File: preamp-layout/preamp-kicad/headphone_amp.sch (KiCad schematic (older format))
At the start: 23 parts, among them J72 Conn_01x04_Male, J73 Conn_01x03_Male, J74 Conn_01x03_Male, J75 Conn_01x03_Male, J76 Conn_01x03_Female, J77 Conn_01x04_Female, U20 TPA6120

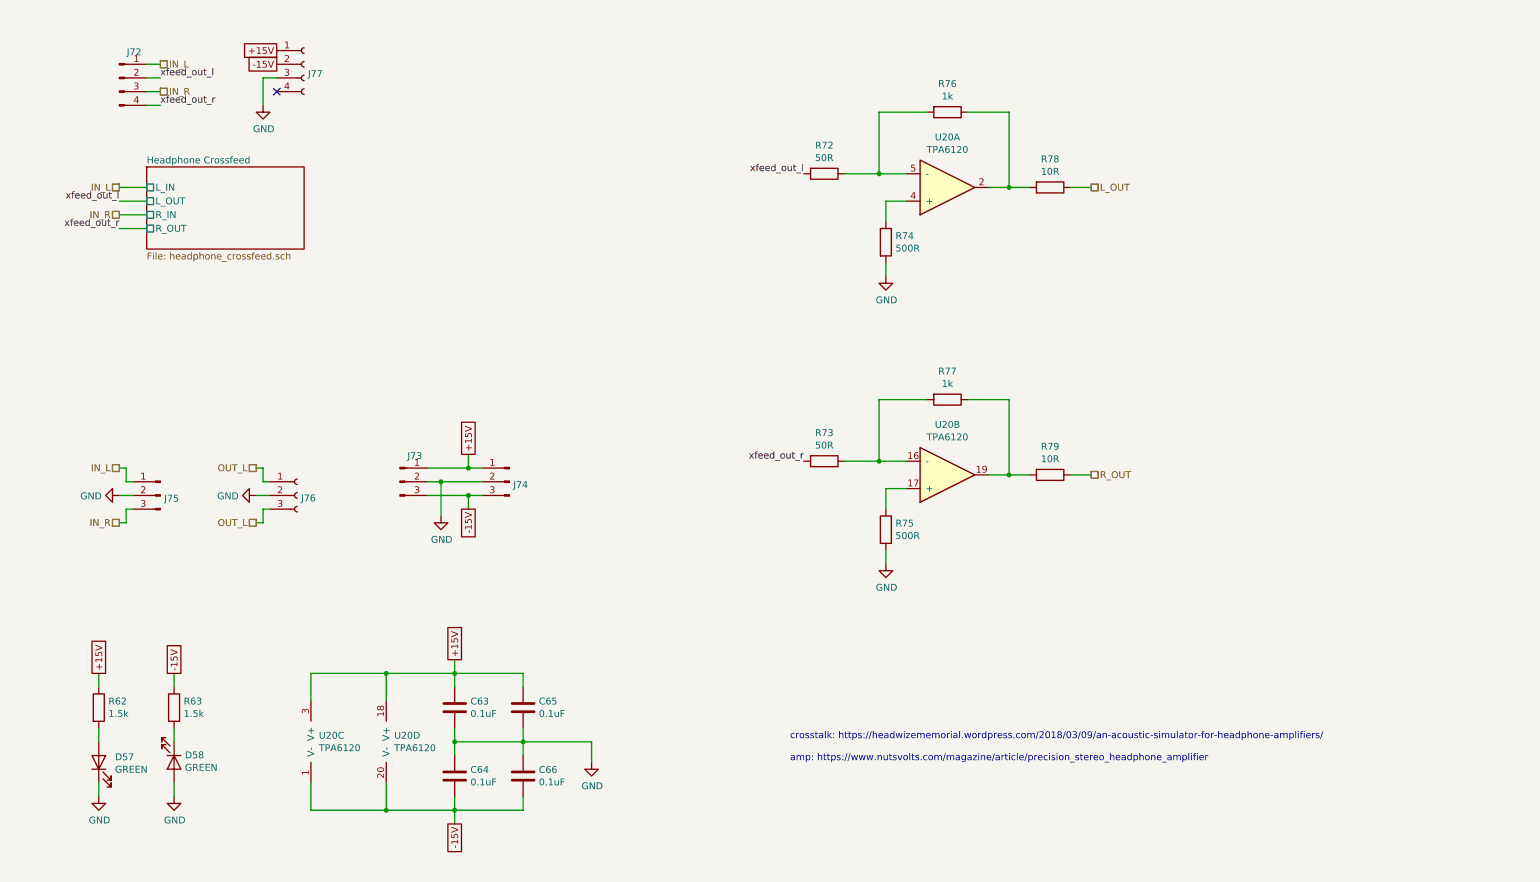
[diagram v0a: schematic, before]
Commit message: Schematic layout updates
schematic optimization. Also implemented encoders with surrounding circuitry (self-contained on encoder board)
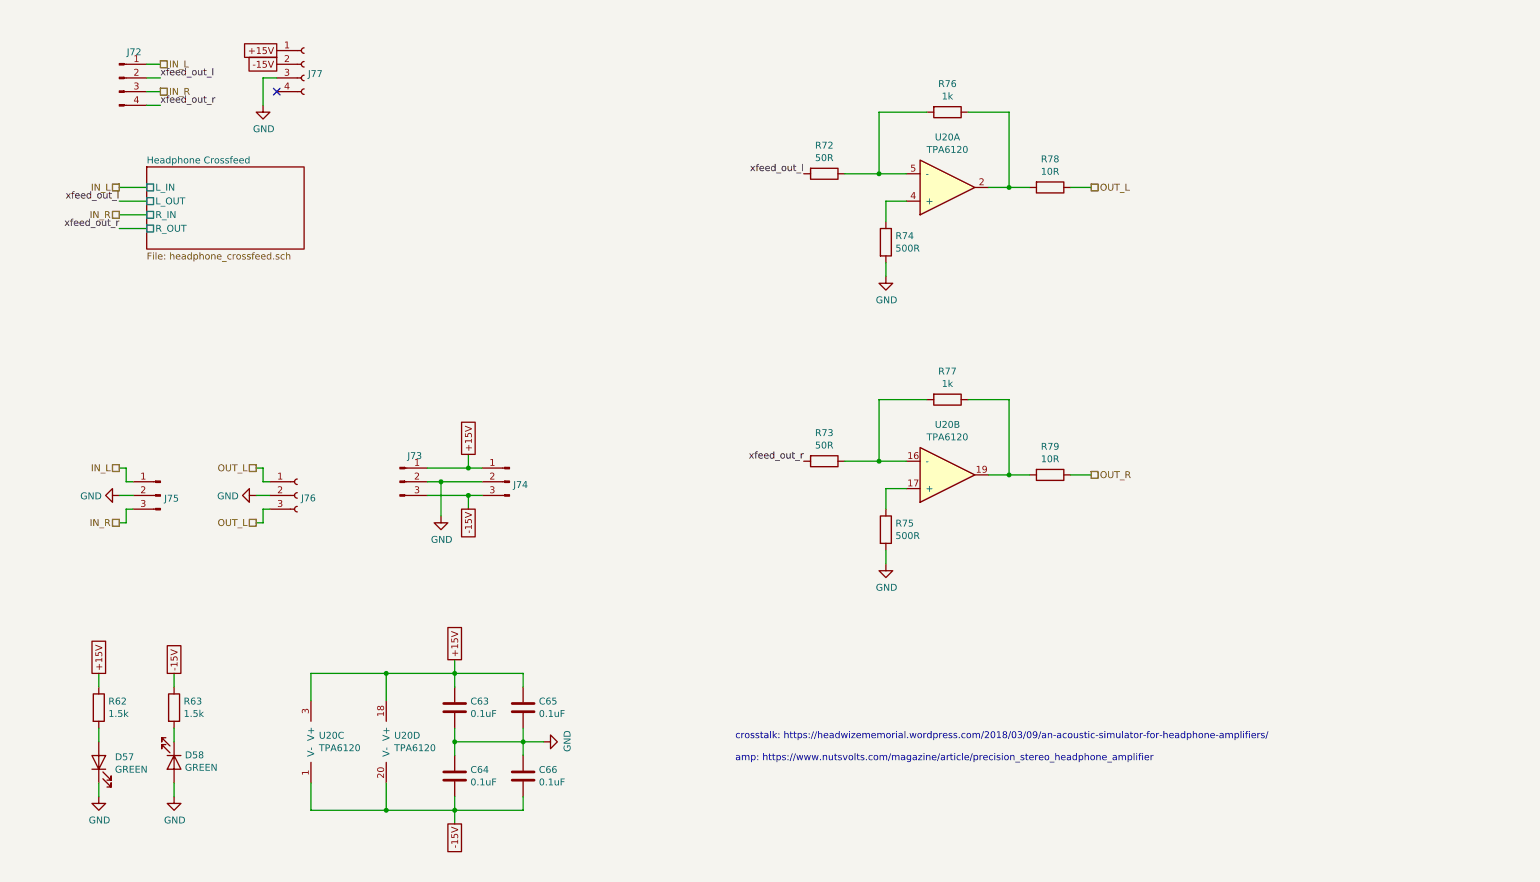
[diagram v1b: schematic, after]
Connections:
- net L_OUT is gone; now on net OUT_L: R78.1
- net R_OUT renamed OUT_R
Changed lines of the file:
@@
 Wire Wire Line
 	8550 4350 8700 4350
-Text Notes 6950 6450 0    50   ~ 0
+Text Notes 6550 6450 0    50   ~ 0
 crosstalk: https://headwizememorial.wordpress.com/2018/03/09/an-acoustic-simulator-for-headphone-amplifiers/\n\namp: https://www.nutsvolts.com/magazine/article/precision_stereo_headphone_amplifier
 Wire Wire Line
@@
 	9000 4350 9150 4350
 Text HLabel 9150 2250 2    50   UnSpc ~ 0
-L_OUT
+OUT_L
 Text HLabel 9150 4350 2    50   UnSpc ~ 0
-R_OUT
+OUT_R
 $Comp
 L preamp:TPA6120 U20
@@
 L power:GND #PWR?
 U 1 1 5F00DE46
-P 5500 6450
+P 5150 6300
 AR Path="/6009D432/5F00DE46" Ref="#PWR?"  Part="1"
 AR Path="/5E4A803E/5F00DE46" Ref="#PWR0142"  Part="1"
-F 0 "#PWR0142" H 5500 6200 50  0001 C CNN
-F 1 "GND" H 5505 6277 50  0000 C CNN
-F 2 "" H 5500 6450 50  0001 C CNN
-F 3 "" H 5500 6450 50  0001 C CNN
-	1    5500 6450
-	1    0    0    -1
+F 0 "#PWR0142" H 5150 6050 50  0001 C CNN
+F 1 "GND" H 5155 6127 50  0000 C CNN
+F 2 "" H 5150 6300 50  0001 C CNN
+F 3 "" H 5150 6300 50  0001 C CNN
+	1    5150 6300
+	0    -1   -1   0
 $EndComp
 Text HLabel 3050 4700 0    50   UnSpc ~ 0
@@
 Wire Wire Line
 	4000 5800 3450 5800
-Wire Wire Line
-	5000 6300 5500 6300
-Wire Wire Line
-	5500 6300 5500 6450
 Text HLabel 2350 1350 2    50   UnSpc ~ 0
 IN_L
@@
 Wire Wire Line
 	4600 4300 4700 4300
+Wire Wire Line
+	5000 6300 5150 6300
 $EndSCHEMATC

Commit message: Sheet cleanup
pin names reassigned, standardized. Organized sheets to reduce clutter, increase readability.
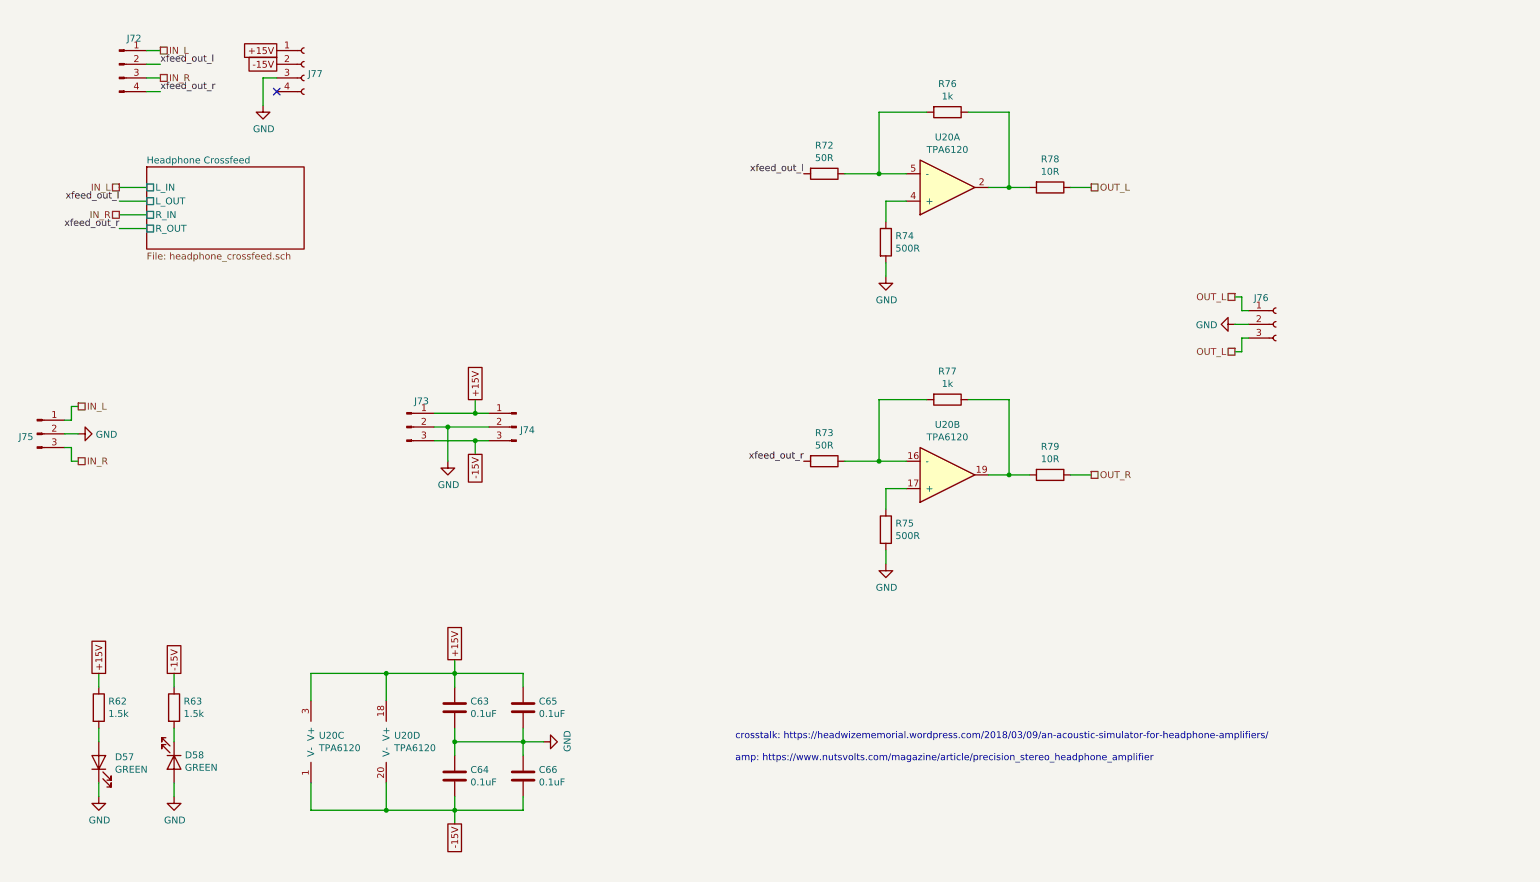
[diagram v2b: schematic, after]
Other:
- moved on the sheet: J72, J73, J74, J75, J76
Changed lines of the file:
@@
 L Connector:Conn_01x03_Male J?
 U 1 1 647A3EBE
-P 4100 4400
+P 4150 4000
 AR Path="/5E27B612/647A3EBE" Ref="J?"  Part="1"
 AR Path="/6009D432/647A3EBE" Ref="J?"  Part="1"
 AR Path="/5E4A803E/647A3EBE" Ref="J73"  Part="1"
-F 0 "J73" H 4208 4589 50  0000 C CNN
-F 1 "Conn_01x03_Male" H 4072 4333 50  0001 R CNN
-F 2 "Connector_JST:JST_EH_B3B-EH-A_1x03_P2.50mm_Vertical" H 4100 4400 50  0001 C CNN
-F 3 "~" H 4100 4400 50  0001 C CNN
-	1    4100 4400
+F 0 "J73" H 4258 4189 50  0000 C CNN
+F 1 "Conn_01x03_Male" H 4122 3933 50  0001 R CNN
+F 2 "Connector_JST:JST_EH_B3B-EH-A_1x03_P2.50mm_Vertical" H 4150 4000 50  0001 C CNN
+F 3 "~" H 4150 4000 50  0001 C CNN
+	1    4150 4000
 	1    0    0    -1
 $EndComp
@@
 L Connector:Conn_01x03_Male J?
 U 1 1 5E7A75D4
-P 4900 4400
+P 4950 4000
 AR Path="/5E27B612/5E7A75D4" Ref="J?"  Part="1"
 AR Path="/6009D432/5E7A75D4" Ref="J?"  Part="1"
 AR Path="/5E4A803E/5E7A75D4" Ref="J74"  Part="1"
-F 0 "J74" H 4872 4378 50  0000 R CNN
-F 1 "Conn_01x03_Male" H 4872 4333 50  0001 R CNN
-F 2 "Connector_JST:JST_EH_B3B-EH-A_1x03_P2.50mm_Vertical" H 4900 4400 50  0001 C CNN
-F 3 "~" H 4900 4400 50  0001 C CNN
-	1    4900 4400
+F 0 "J74" H 4922 3978 50  0000 R CNN
+F 1 "Conn_01x03_Male" H 4922 3933 50  0001 R CNN
+F 2 "Connector_JST:JST_EH_B3B-EH-A_1x03_P2.50mm_Vertical" H 4950 4000 50  0001 C CNN
+F 3 "~" H 4950 4000 50  0001 C CNN
+	1    4950 4000
 	-1   0    0    -1
 $EndComp
@@
 	0    -1   -1   0
 $EndComp
-Text HLabel 3050 4700 0    50   UnSpc ~ 0
+Text HLabel 10200 3450 0    50   UnSpc ~ 0
 OUT_L
-Text HLabel 3050 4300 0    50   UnSpc ~ 0
+Text HLabel 10200 3050 0    50   UnSpc ~ 0
 OUT_L
 $Comp
 L power:GND #PWR?
 U 1 1 5F3ED77C
-P 3050 4500
+P 10200 3250
 AR Path="/5E26F6FE/5F3ED77C" Ref="#PWR?"  Part="1"
 AR Path="/5E4A803E/5F3ED77C" Ref="#PWR0102"  Part="1"
-F 0 "#PWR0102" H 3050 4250 50  0001 C CNN
-F 1 "GND" V 3055 4372 50  0000 R CNN
-F 2 "" H 3050 4500 50  0001 C CNN
-F 3 "" H 3050 4500 50  0001 C CNN
-	1    3050 4500
+F 0 "#PWR0102" H 10200 3000 50  0001 C CNN
+F 1 "GND" V 10205 3122 50  0000 R CNN
+F 2 "" H 10200 3250 50  0001 C CNN
+F 3 "" H 10200 3250 50  0001 C CNN
+	1    10200 3250
 	0    1    1    0
 $EndComp
 Wire Wire Line
-	3100 4700 3050 4700
-Wire Wire Line
-	3100 4600 3100 4700
-Wire Wire Line
-	3150 4600 3100 4600
-Wire Wire Line
-	3100 4300 3050 4300
-Wire Wire Line
-	3100 4400 3100 4300
-Wire Wire Line
-	3150 4400 3100 4400
-Wire Wire Line
-	3150 4500 3050 4500
+	10250 3450 10200 3450
+Wire Wire Line
+	10250 3350 10250 3450
+Wire Wire Line
+	10300 3350 10250 3350
+Wire Wire Line
+	10250 3050 10200 3050
+Wire Wire Line
+	10250 3150 10250 3050
+Wire Wire Line
+	10300 3150 10250 3150
+Wire Wire Line
+	10300 3250 10200 3250
 $Comp
 L Connector:Conn_01x03_Female J?
 U 1 1 5F33E58A
-P 3350 4500
+P 10500 3250
 AR Path="/5E607732/5F33E58A" Ref="J?"  Part="1"
 AR Path="/5E2D8DA2/5F33E58A" Ref="J?"  Part="1"
 AR Path="/6009D432/5F33E58A" Ref="J?"  Part="1"
 AR Path="/5E4A803E/5F33E58A" Ref="J76"  Part="1"
-F 0 "J76" H 3378 4480 50  0000 L CNN
-F 1 "Conn_01x03_Female" H 3378 4435 50  0001 L CNN
-F 2 "Connector_PinHeader_2.54mm:PinHeader_1x03_P2.54mm_Vertical" H 3350 4500 50  0001 C CNN
-F 3 "~" H 3350 4500 50  0001 C CNN
-	1    3350 4500
+F 0 "J76" H 10392 3443 50  0000 C CNN
+F 1 "Conn_01x03_Female" H 10528 3185 50  0001 L CNN
+F 2 "Connector_PinHeader_2.54mm:PinHeader_1x03_P2.54mm_Vertical" H 10500 3250 50  0001 C CNN
+F 3 "~" H 10500 3250 50  0001 C CNN
+	1    10500 3250
 	1    0    0    -1
 $EndComp
@@
 L power:GND #PWR?
 U 1 1 5F1B4E90
-P 2050 4500
+P 1750 4050
 AR Path="/5E26F6FE/5F1B4E90" Ref="#PWR?"  Part="1"
 AR Path="/5E4A803E/5F1B4E90" Ref="#PWR099"  Part="1"
-F 0 "#PWR099" H 2050 4250 50  0001 C CNN
-F 1 "GND" V 2055 4372 50  0000 R CNN
-F 2 "" H 2050 4500 50  0001 C CNN
-F 3 "" H 2050 4500 50  0001 C CNN
-	1    2050 4500
-	0    1    1    0
-$EndComp
-Wire Wire Line
-	2100 4700 2050 4700
-Wire Wire Line
-	2100 4600 2100 4700
-Wire Wire Line
-	2150 4600 2100 4600
-Wire Wire Line
-	2100 4300 2050 4300
-Wire Wire Line
-	2100 4400 2100 4300
-Wire Wire Line
-	2150 4400 2100 4400
+F 0 "#PWR099" H 1750 3800 50  0001 C CNN
+F 1 "GND" V 1755 3922 50  0000 R CNN
+F 2 "" H 1750 4050 50  0001 C CNN
+F 3 "" H 1750 4050 50  0001 C CNN
+	1    1750 4050
+	0    -1   1    0
+$EndComp
+Wire Wire Line
+	1700 4250 1750 4250
+Wire Wire Line
+	1700 4150 1700 4250
+Wire Wire Line
+	1650 4150 1700 4150
+Wire Wire Line
+	1700 3850 1750 3850
+Wire Wire Line
+	1700 3950 1700 3850
+Wire Wire Line
+	1650 3950 1700 3950
 $Comp
 L Connector:Conn_01x03_Male J?
 U 1 1 5F1B4E80
-P 2350 4500
+P 1450 4050
 AR Path="/5E27B612/5F1B4E80" Ref="J?"  Part="1"
 AR Path="/6009D432/5F1B4E80" Ref="J?"  Part="1"
 AR Path="/5E4A803E/5F1B4E80" Ref="J75"  Part="1"
-F 0 "J75" H 2322 4478 50  0000 R CNN
-F 1 "Conn_01x03_Male" H 2322 4433 50  0001 R CNN
-F 2 "Connector_PinHeader_2.54mm:PinHeader_1x03_P2.54mm_Vertical" H 2350 4500 50  0001 C CNN
-F 3 "~" H 2350 4500 50  0001 C CNN
-	1    2350 4500
-	-1   0    0    -1
-$EndComp
-Wire Wire Line
-	2150 4500 2050 4500
-Text HLabel 2050 4300 0    50   UnSpc ~ 0
+F 0 "J75" H 1422 4028 50  0000 R CNN
+F 1 "Conn_01x03_Male" H 1422 3983 50  0001 R CNN
+F 2 "Connector_PinHeader_2.54mm:PinHeader_1x03_P2.54mm_Vertical" H 1450 4050 50  0001 C CNN
+F 3 "~" H 1450 4050 50  0001 C CNN
+	1    1450 4050
+	1    0    0    -1
+$EndComp
+Wire Wire Line
+	1650 4050 1750 4050
+Text HLabel 1750 3850 2    50   UnSpc ~ 0
 IN_L
-Text HLabel 2050 4700 0    50   UnSpc ~ 0
+Text HLabel 1750 4250 2    50   UnSpc ~ 0
 IN_R
 $Comp
@@
 L Connector:Conn_01x04_Male J72
 U 1 1 5E6D1CB1
-P 2050 1450
-F 0 "J72" H 2158 1639 50  0000 C CNN
-F 1 "Conn_01x04_Male" H 2158 1640 50  0001 C CNN
-F 2 "Connector_PinHeader_2.54mm:PinHeader_1x04_P2.54mm_Vertical" H 2050 1450 50  0001 C CNN
-F 3 "~" H 2050 1450 50  0001 C CNN
-	1    2050 1450
+P 2050 1350
+F 0 "J72" H 2158 1539 50  0000 C CNN
+F 1 "Conn_01x04_Male" H 2158 1540 50  0001 C CNN
+F 2 "Connector_PinHeader_2.54mm:PinHeader_1x04_P2.54mm_Vertical" H 2050 1350 50  0001 C CNN
+F 3 "~" H 2050 1350 50  0001 C CNN
+	1    2050 1350
 	1    0    0    -1
 $EndComp
@@
 Wire Wire Line
 	3200 1450 3100 1450
-Text GLabel 4600 4200 1    50   UnSpc ~ 0
+Text GLabel 4650 3800 1    50   UnSpc ~ 0
 +15V
-Text GLabel 4600 4600 3    50   UnSpc ~ 0
+Text GLabel 4650 4200 3    50   UnSpc ~ 0
 -15V
 $Comp
 L power:GND #PWR?
 U 1 1 601F478F
-P 4400 4650
+P 4450 4250
 AR Path="/6009D432/601F478F" Ref="#PWR?"  Part="1"
 AR Path="/5E4A803E/601F478F" Ref="#PWR0106"  Part="1"
-F 0 "#PWR0106" H 4400 4400 50  0001 C CNN
-F 1 "GND" H 4405 4477 50  0000 C CNN
-F 2 "" H 4400 4650 50  0001 C CNN
-F 3 "" H 4400 4650 50  0001 C CNN
-	1    4400 4650
-	1    0    0    -1
-$EndComp
-Wire Wire Line
-	4300 4500 4600 4500
-Wire Wire Line
-	4600 4600 4600 4500
+F 0 "#PWR0106" H 4450 4000 50  0001 C CNN
+F 1 "GND" H 4455 4077 50  0000 C CNN
+F 2 "" H 4450 4250 50  0001 C CNN
+F 3 "" H 4450 4250 50  0001 C CNN
+	1    4450 4250
+	1    0    0    -1
+$EndComp
+Wire Wire Line
+	4350 4100 4650 4100
+Wire Wire Line
+	4650 4200 4650 4100
 Wire Wire Line
 	4500 6800 4000 6800
@@
 Wire Wire Line
 	4000 5800 3450 5800
-Text HLabel 2350 1350 2    50   UnSpc ~ 0
+Text HLabel 2350 1250 2    50   UnSpc ~ 0
 IN_L
-Text HLabel 2350 1550 2    50   UnSpc ~ 0
+Text HLabel 2350 1450 2    50   UnSpc ~ 0
 IN_R
-Text Label 2350 1450 0    50   ~ 0
+Text Label 2350 1350 0    50   ~ 0
 xfeed_out_l
-Text Label 2350 1650 0    50   ~ 0
+Text Label 2350 1550 0    50   ~ 0
 xfeed_out_r
 Wire Wire Line
+	2250 1250 2350 1250
+Wire Wire Line
 	2250 1350 2350 1350
 Wire Wire Line
@@
 	2250 1550 2350 1550
 Wire Wire Line
-	2250 1650 2350 1650
-Wire Wire Line
 	2050 2250 2250 2250
 Wire Wire Line
@@
 	2050 2550 2250 2550
 Wire Wire Line
-	4300 4300 4600 4300
-Wire Wire Line
-	4300 4400 4400 4400
-Wire Wire Line
-	4400 4650 4400 4400
-Connection ~ 4400 4400
-Connection ~ 4600 4500
-Wire Wire Line
-	4600 4500 4700 4500
-Wire Wire Line
-	4400 4400 4700 4400
-Wire Wire Line
-	4600 4200 4600 4300
-Connection ~ 4600 4300
-Wire Wire Line
-	4600 4300 4700 4300
+	4350 3900 4650 3900
+Wire Wire Line
+	4350 4000 4450 4000
+Wire Wire Line
+	4450 4250 4450 4000
+Connection ~ 4450 4000
+Connection ~ 4650 4100
+Wire Wire Line
+	4650 4100 4750 4100
+Wire Wire Line
+	4450 4000 4750 4000
+Wire Wire Line
+	4650 3800 4650 3900
+Connection ~ 4650 3900
+Wire Wire Line
+	4650 3900 4750 3900
 Wire Wire Line
 	5000 6300 5150 6300

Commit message: BOM Update
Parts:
- R74, R75: value 500R -> 499R
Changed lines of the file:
@@
 AR Path="/5E4A803E/5F1C3374" Ref="R74"  Part="1"
 F 0 "R74" H 7720 2696 50  0000 L CNN
-F 1 "500R" H 7720 2605 50  0000 L CNN
+F 1 "499R" H 7720 2605 50  0000 L CNN
 F 2 "Resistor_SMD:R_1206_3216Metric_Pad1.42x1.75mm_HandSolder" V 7580 2650 50  0001 C CNN
 F 3 "~" H 7650 2650 50  0001 C CNN
@@
 AR Path="/5E4A803E/5F1D9CED" Ref="R75"  Part="1"
 F 0 "R75" H 7720 4796 50  0000 L CNN
-F 1 "500R" H 7720 4705 50  0000 L CNN
+F 1 "499R" H 7720 4705 50  0000 L CNN
 F 2 "Resistor_SMD:R_1206_3216Metric_Pad1.42x1.75mm_HandSolder" V 7580 4750 50  0001 C CNN
 F 3 "~" H 7650 4750 50  0001 C CNN
